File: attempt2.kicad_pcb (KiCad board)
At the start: 2 copper layers, 72 x 58.8 mm, 71 parts, among them J1 SIM_Card, J3 U.FL-R-SMT-110, J4 USB_C_Receptacle_USB2.0_14P, J5 U.FL-R-SMT-110, SW3 SW_Push, SW4 SW_Push, U1 nRF9160-SIxA, U2 TPD3F303DPVR, U3 MCP73831T-2ACI_OT, U4 MIC94092YC6-TR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

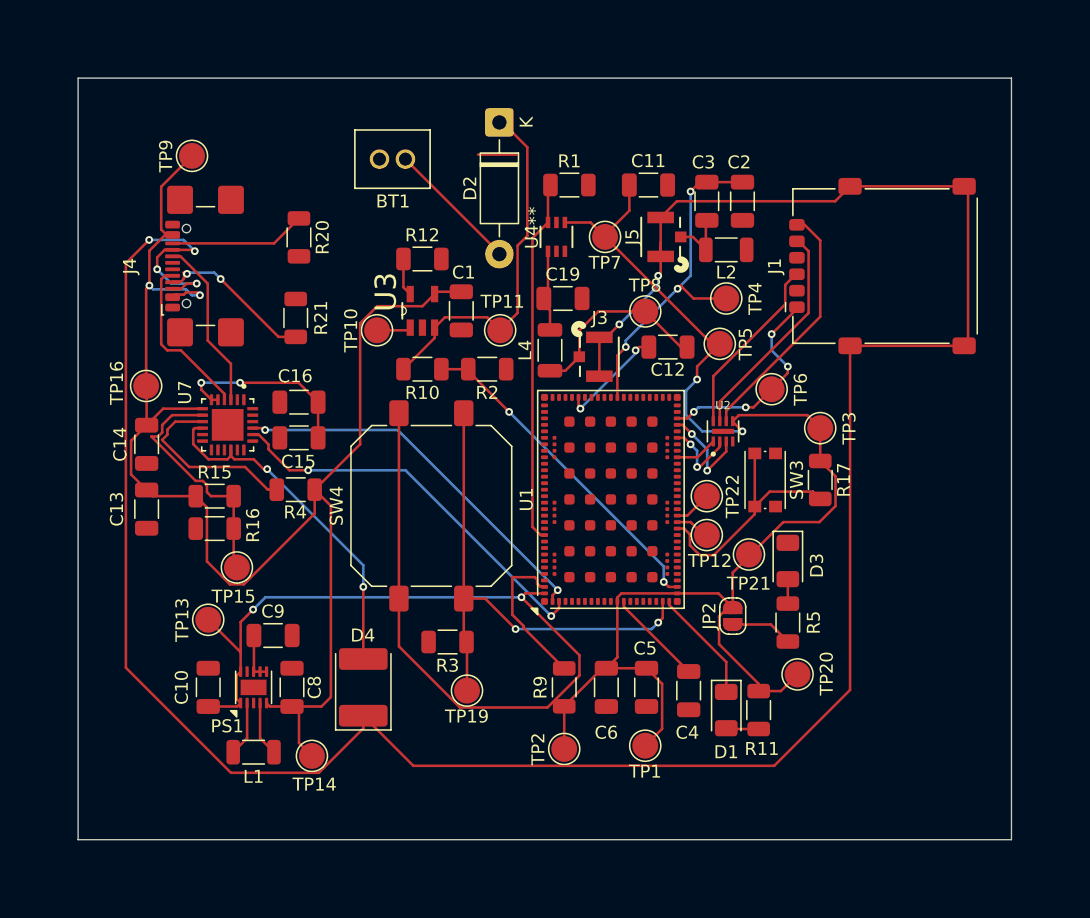
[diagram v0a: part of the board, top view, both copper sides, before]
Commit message: flipped direction of usb and moved antennas to edge
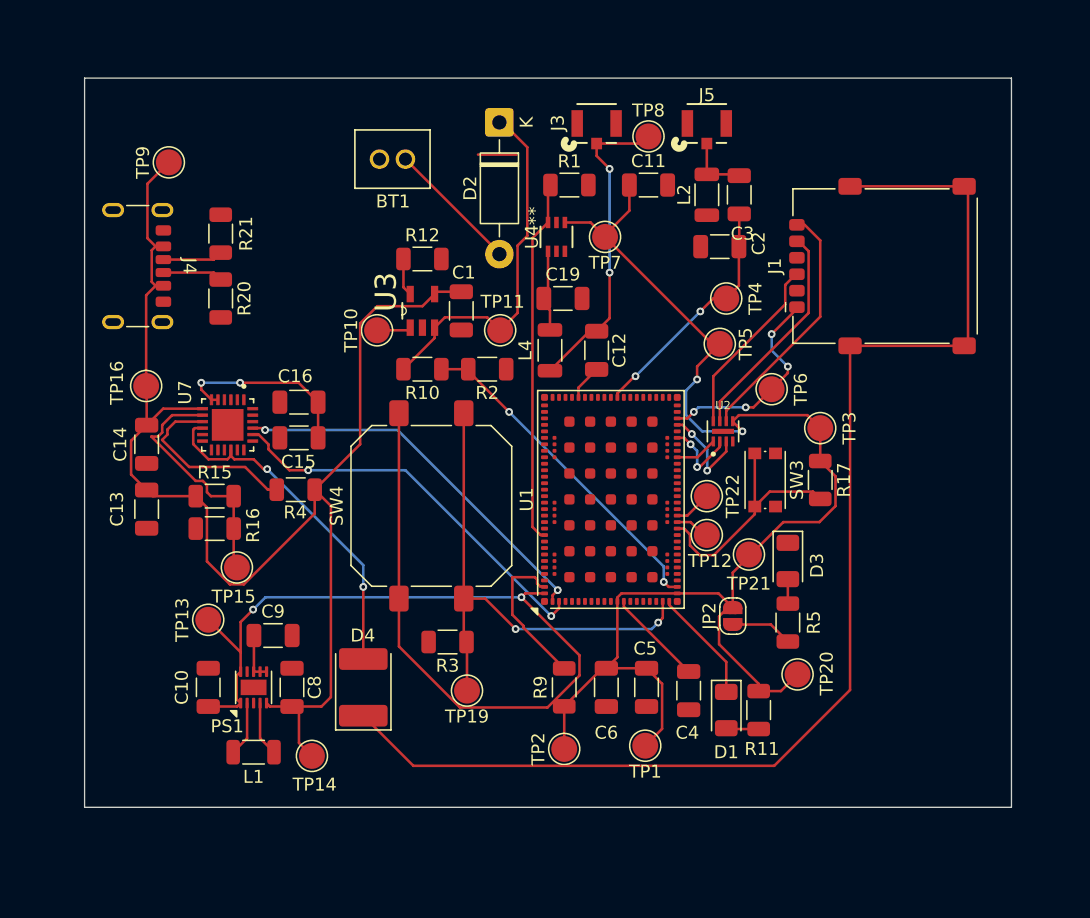
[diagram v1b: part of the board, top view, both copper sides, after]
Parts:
- J4: footprint Connector_USB:USB_C_Receptacle_GCT_USB4110 -> Connector_USB:USB_C_Receptacle_GCT_USB4125-xx-x-0190_6P_TopMnt_Horizontal
- R10, R2: value R -> 100k
- R11, R5: value R -> 500k
- R15: value 100k -> 22k
- R16: value 100k -> 33k
- R17: value 100k -> 1k
- R3: value 100k -> 10k
- R9: value 1M -> 10k
- moved J3 18.0 mm to (140.5, 82.0), turned to 0 degrees
- moved TP8 13.5 mm to (144.5, 83.0)
- moved J5 9.45 mm to (149.0, 82.0), turned to 0 degrees
- moved R21 8.70 mm to (111.5, 90.5)
- moved R20 7.66 mm to (111.5, 95.5)
- moved J4 7.47 mm to (104.0, 93.0), turned to -90 degrees
- moved C12 5.51 mm to (140.5, 99.5), turned to 90 degrees
- moved L2 4.51 mm to (149.0, 87.5), turned to -90 degrees
- moved C2 3.91 mm to (150.0, 91.5), turned to 180 degrees
- moved C3 2.55 mm to (151.5, 87.5), turned to -90 degrees
- moved TP9 1.86 mm to (107.5, 85.0)
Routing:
- net (no net): track 227.5 -> 125.1 mm, vias 8 -> 2
- net DIFF_P: track 13.3 -> 0.00 mm
- net DIFF_N: track 12.9 -> 0.00 mm
- net Net-(C12-Pad2): track 14.8 -> 24.4 mm, vias 0 -> 2
- net Net-(U1-ANT): track 26.8 -> 18.7 mm, vias 3 -> 2
- net Net-(J4-CC1): track 12.5 -> 4.64 mm, vias 2 -> 0
- net VBUS: track 112.7 -> 105.6 mm, vias 2 -> 0
- net Net-(J4-CC2): track 10.5 -> 4.64 mm
- net GPS: track 8.43 -> 2.73 mm, vias 2 -> 0
- net Net-(C3-Pad1): track 4.26 -> 4.92 mm
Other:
- board size 72 x 58.8 mm -> 71.5 x 56.2 mm

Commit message: worked on erc and drc errors
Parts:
- removed C11: C, Capacitor_SMD:C_1206_3216Metric
- removed TP5, TP6: TestPoint, TestPoint:TestPoint_Pad_D2.0mm
- added C7: 100n, Capacitor_SMD:C_1206_3216Metric, F.Cu at (164.0, 101.5)
- J1: footprint Connector_Card:nanoSIM_GCT_SIM8060-6-1-14-00 -> Connector_Card:nanoSIM_GCT_SIM8060-6-0-14-00
- J4: footprint Connector_USB:USB_C_Receptacle_GCT_USB4125-xx-x-0190_6P_TopMnt_Horizontal -> Connector_USB:USB_C_Receptacle_GCT_USB4110
- R10, R2: value 100k -> R
- R11, R5: value 500k -> R
- R15: value 22k -> 100k
- R16: value 33k -> 100k
- R17: value 1k -> 100k
- R3: value 10k -> 100k
- R9: value 10k -> 1M
- moved R20 1.50 mm to (113.0, 95.5)
- moved R21 1.50 mm to (113.0, 90.5)
- moved TP9 1.50 mm to (107.5, 83.5)
- turned U2 to 180 degrees
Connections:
- U2 pad 1: Net-(U1-SIM_RST) -> Net-(J1-RST)
- U2 pad 2: Net-(U1-SIM_CLK) -> Net-(J1-CLK)
- U2 pad 3: Net-(U1-SIM_IO) -> Net-(J1-I/O)
- U2 pad 5: VSYS -> Net-(J1-VCC)
- U2 pad 6: Net-(J1-I/O) -> Net-(U1-SIM_IO)
- U2 pad 7: Net-(J1-CLK) -> Net-(U1-SIM_CLK)
- U2 pad 8: Net-(J1-RST) -> Net-(U1-SIM_RST)
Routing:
- net GND: track 3.00 -> 161.7 mm, vias 0 -> 23
- net DIFF_N: track 0.00 -> 15.8 mm, vias 0 -> 2
- net DIFF_P: track 0.00 -> 14.9 mm, vias 0 -> 2
- net VSYS: track 184.6 -> 172.0 mm
- net Net-(J1-VCC): track 16.4 -> 24.9 mm, vias 4 -> 6
- net VBUS: track 105.6 -> 110.5 mm
- net Net-(U1-SIM_IO): track 7.59 -> 2.85 mm, vias 2 -> 0
- net Net-(U1-SIM_CLK): track 6.01 -> 2.85 mm, vias 2 -> 0
- net Net-(J1-RST): track 14.1 -> 17.1 mm
- net Net-(J1-CLK): track 17.2 -> 18.5 mm, vias 0 -> 2
- net Net-(PS1-EN): track 3.80 -> 4.94 mm
- net Net-(J4-CC2): track 4.64 -> 5.62 mm
- net Net-(U7-VDD): track 14.5 -> 15.4 mm
- net Net-(J4-CC1): track 4.64 -> 5.41 mm
- net Net-(J1-I/O): track 19.3 -> 19.9 mm

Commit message: final cleanup before design review
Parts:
- C7: value 100n -> 1n
- R20: value 1.5k -> 5.1k
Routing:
- net DIFF_P: track 14.9 -> 17.3 mm
- net GND: track 161.7 -> 159.5 mm
- net DIFF_N: track 15.8 -> 17.2 mm, vias 2 -> 4
- net VBUS: track 110.5 -> 109.2 mm

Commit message: FINAL BEFORE ANDREW
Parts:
- removed TP12: SWDCLK, TestPoint:TestPoint_Pad_D2.0mm
- removed TP22: SWDIO, TestPoint:TestPoint_Pad_D2.0mm
- added J2: Conn_01x05_Pin, Connector_PinSocket_2.54mm:PinSocket_1x05_P2.54mm_Vertical, F.Cu at (163.0, 115.7)
- R15: value 100k -> 22k
- R16: value 100k -> 33k
- moved R17 1.25 mm to (156.5, 109.5)
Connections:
- R17 pad 2: Net-(U1-~{RESET}) -> Net-(J2-Pin_5)
- SW3 pad 1: GND -> Net-(J2-Pin_5)
- SW3 pad 2: Net-(U1-~{RESET}) -> GND
- U1 pad 32: Net-(U1-~{RESET}) -> Net-(J2-Pin_5)
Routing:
- net Net-(J2-Pin_5): track 0.00 -> 26.0 mm, vias 0 -> 2
- net Net-(U1-~{RESET}): track 19.1 -> 0.00 mm
- net Net-(J2-Pin_4): track 2.90 -> 18.0 mm, vias 0 -> 2
- net Net-(J2-Pin_2): track 2.80 -> 16.5 mm, vias 0 -> 2
- net VSYS: track 172.0 -> 181.5 mm, vias 4 -> 6
- net GND: track 159.5 -> 165.1 mm, vias 23 -> 24
- net DIFF_N: track 17.2 -> 19.5 mm
- net VBUS: track 109.2 -> 110.3 mm
- net DIFF_P: track 17.3 -> 18.0 mm
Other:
- board text added: "STAT BOARD v1.0"

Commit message: fixed resistor values
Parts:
- R10, R2: value R -> 100k
- R11, R5: value R -> 500
- R17: value 100k -> 1k
- R3: value 100k -> 4.7k
- R9: value 1M -> 10k
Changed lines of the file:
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@@
 			)
 		)
-		(property "Value" "R"
+		(property "Value" "100k"
 			(at 0 1.83 0)
 			(layer "F.Fab")
@@
 			)
 		)
-		(property "Value" "100k"
+		(property "Value" "4.7k"
 			(at 0 1.83 0)
 			(layer "F.Fab")
@@
 			)
 		)
-		(property "Value" "R"
+		(property "Value" "100k"
 			(at 0 1.83 0)
 			(layer "F.Fab")
@@
 			)
 		)
-		(property "Value" "R"
+		(property "Value" "500"
 			(at 0 1.83 90)
 			(layer "F.Fab")
@@
 			)
 		)
-		(property "Value" "100k"
+		(property "Value" "1k"
 			(at 0 1.83 90)
 			(layer "F.Fab")
@@
 			)
 		)
-		(property "Value" "R"
+		(property "Value" "500"
 			(at 0 1.83 90)
 			(layer "F.Fab")
@@
 			)
 		)
-		(property "Value" "1M"
+		(property "Value" "10k"
 			(at 0 1.83 90)
 			(layer "F.Fab")

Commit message: rah
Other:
- board text added: "STAT BOARD 8/2/2025 v1.0"
- board text removed: "STAT BOARD v1.0"
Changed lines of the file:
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@@
 	)
 	(paper "A4")
+	(title_block
+		(title "STAT BOARD")
+		(date "2025-08-02")
+		(rev "v1.0")
+		(company "XIBIDI TECHNOLOGIES")
+	)
 	(layers
 		(0 "F.Cu" signal)
@@
 		(layer "Edge.Cuts")
 	)
-	(gr_text "STAT BOARD\nv1.0"
+	(gr_text "STAT BOARD\n8/2/2025\nv1.0"
 		(at 170.5 133 0)
 		(layer "F.SilkS")

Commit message: Schematic design review, remove 3.3V switcher and run right off battery, re-arrange schematic for easier reading, moved to four layer PCB because RF, cleaned up zones, including adding vbat zone. Plenty left to do, see design review notes.
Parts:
- removed C10: 100u, Capacitor_SMD:C_1206_3216Metric
- removed C8: 10u, Capacitor_SMD:C_1206_3216Metric
- removed C9: 100p, Capacitor_SMD:C_1206_3216Metric
- removed D2: SB120, Diode_THT:D_DO-41_SOD81_P10.16mm_Horizontal
- removed D4: BAT20JFILM, Diode_SMD:D_2114_3652Metric
- removed L1: 1.5u, Inductor_SMD:L_1206_3216Metric
- removed PS1: TPS63031DSKR, Package_SON:WSON-10-1EP_2.5x2.5mm_P0.5mm_EP1.2x2mm
- removed R15: 22k, Resistor_SMD:R_1206_3216Metric
- removed R16: 33k, Resistor_SMD:R_1206_3216Metric
- removed R17: 1k, Resistor_SMD:R_1206_3216Metric
- removed TP13, TP14, TP8: TestPoint, TestPoint:TestPoint_Pad_D2.0mm
- added C11: 100n, Capacitor_SMD:C_1206_3216Metric, F.Cu at (95.8, 110.8)
- BT1: value Battery_Cell -> 1528-2731-ND
- R11, R5: value 500 -> 2k
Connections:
- BT1 pad 1: Net-(BT1-+) -> +3V8
- C5 pad 1: VSYS -> +3V8
- C6 pad 1: VSYS -> +3V8
- J2 pad 1: VSYS -> +3V8
- J4 pad S1: GND -> Net-(J4-SHIELD)
- JP2 pad 2: VSYS -> +3V8
- R10 pad 2: VBAT -> +3V8
- R11 pad 1: VSYS -> +3V8
- R9 pad 1: VSYS -> +3V8
- SW4 pad 1: VSYS -> +3V8
- TP1 pad 1: VSYS -> +3V8
- TP11 pad 1: VBAT -> +3V8
- TP15 pad 1: Net-(U7-VBUS) -> VBUS
- TP2 pad 1: VSYS -> +3V8
- TP20 pad 1: VSYS -> +3V8
- TP21 pad 1: VSYS -> +3V8
- TP3 pad 1: VSYS -> Net-(J2-Pin_5)
- TP7 pad 1: VSYS -> +3V8
- U1 pad 102: VSYS -> +3V8
- U1 pad 12: VSYS -> +3V8
- U1 pad 22: VSYS -> +3V8
- U3 pad 3: VBAT -> +3V8
- U4 pad 4: VSYS -> +3V8
- U7 pad 8: Net-(U7-VBUS) -> VBUS
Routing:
- net VSYS: track 181.5 -> 0.00 mm, vias 6 -> 0
- net (no net): track 125.1 -> 209.0 mm
- net VBAT: track 27.9 -> 0.00 mm
- net +3V8: track 0.00 -> 19.2 mm, vias 0 -> 6
- net Net-(U7-VBUS): track 19.2 -> 0.00 mm
- net Net-(BT1-+): track 10.6 -> 0.00 mm
- net GND: track 165.1 -> 155.2 mm, vias 24 -> 32
- net VBUS: track 110.3 -> 105.1 mm
- net Net-(PS1-EN): track 4.94 -> 0.00 mm
- net Net-(PS1-L1): track 4.48 -> 0.00 mm
- net Net-(PS1-L2): track 4.23 -> 0.00 mm
- net DIFF_N: track 19.5 -> 15.6 mm, vias 4 -> 2
- added copper zone on In2.Cu, net +3V8
- added copper zone on In1.Cu, net GND
- added copper zone on In2.Cu, net GND
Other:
- copper layers 2 -> 4

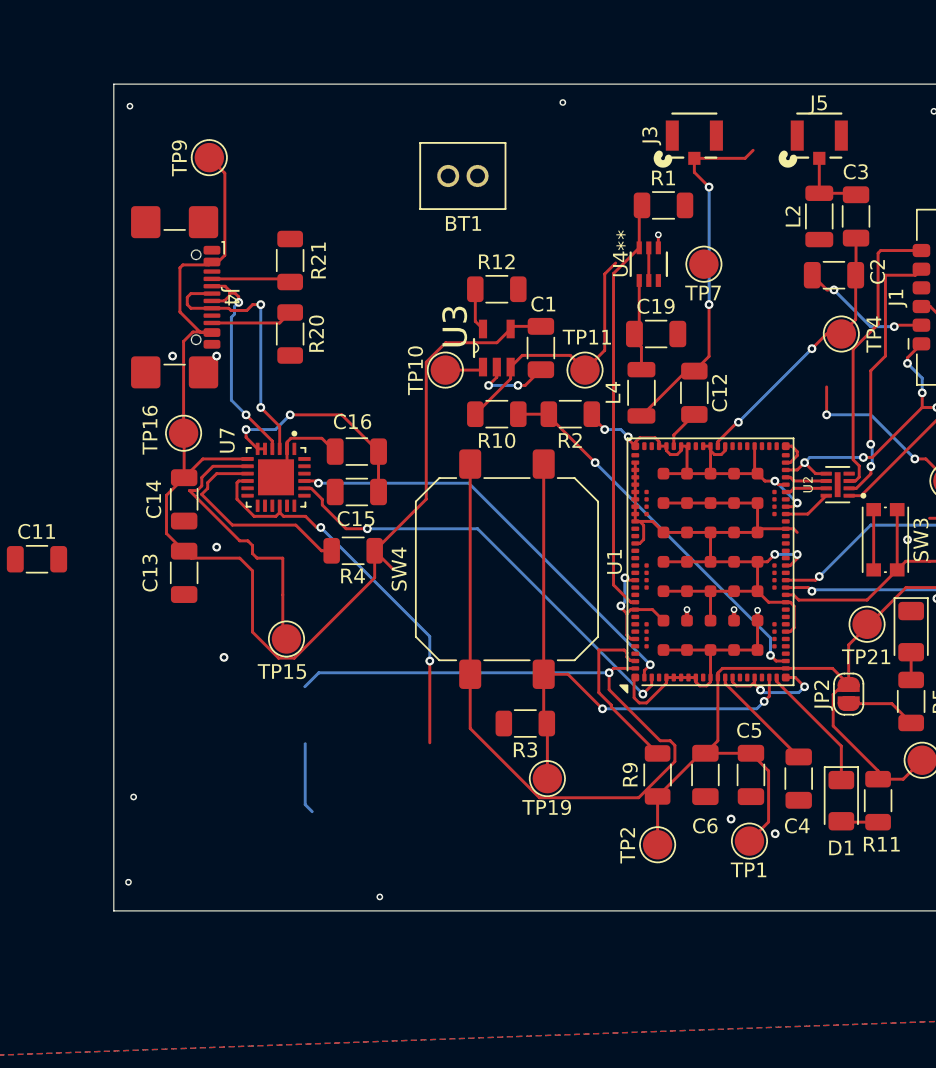
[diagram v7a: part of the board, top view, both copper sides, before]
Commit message: changed gps antenna lte antenna xibidi and other thins too
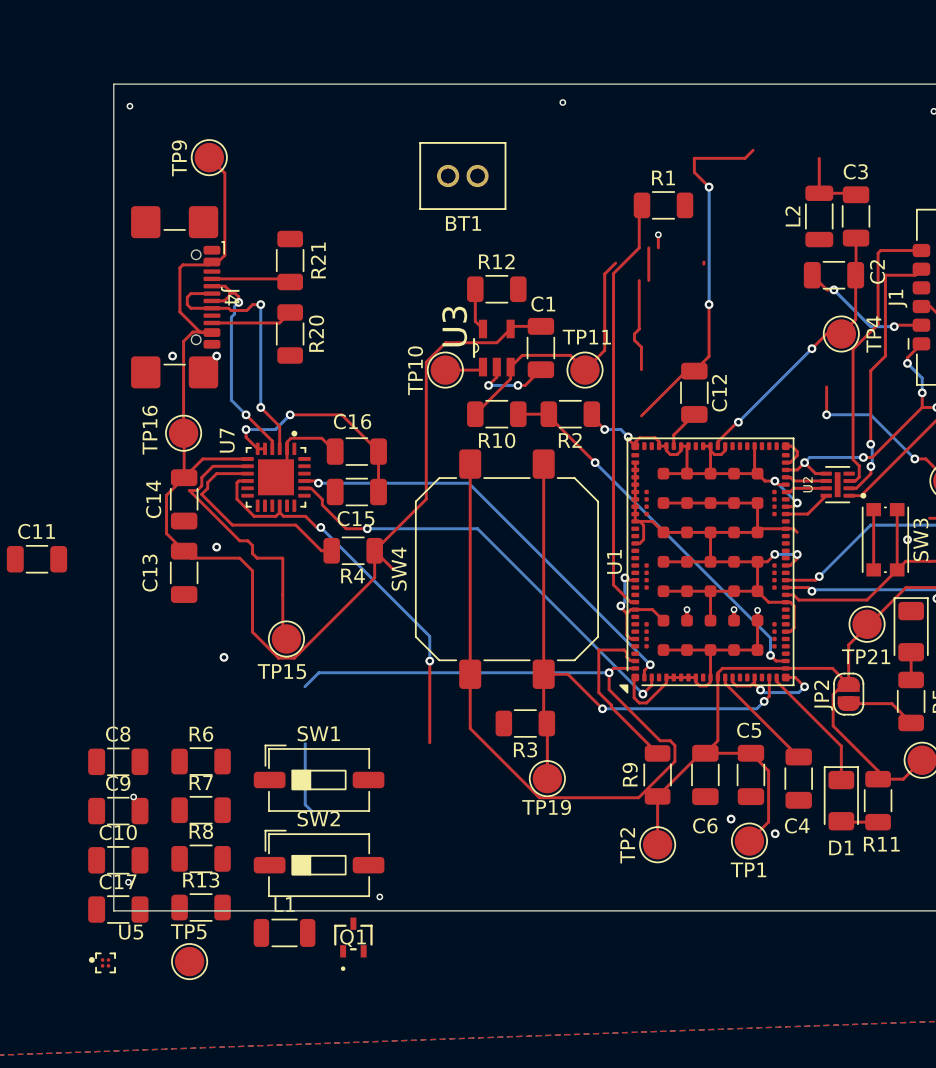
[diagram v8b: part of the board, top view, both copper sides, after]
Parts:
- removed C19: 56p, Capacitor_SMD:C_1206_3216Metric
- removed J3, J5: U.FL-R-SMT-110, footprints:CONN1_UFL-R_HIR
- removed L4: 68n, Inductor_SMD:L_1206_3216Metric
- removed TP7: TestPoint, TestPoint:TestPoint_Pad_D2.0mm
- removed U4: MIC94092YC6-TR, footprints:SC-70-6_C6_MCH
- added C10: 47u, Capacitor_SMD:C_1206_3216Metric, F.Cu at (101.3, 131.3)
- added C17: 4.7u, Capacitor_SMD:C_1206_3216Metric, F.Cu at (101.3, 134.7)
- added C8: 100nF, Capacitor_SMD:C_1206_3216Metric, F.Cu at (101.3, 124.6)
- added C9: 10p, Capacitor_SMD:C_1206_3216Metric, F.Cu at (101.3, 128.0)
- added L1: 7.3n, Inductor_SMD:L_1206_3216Metric, F.Cu at (112.6, 136.2)
- added Q1: PMOS, footprints_mosfet:SOT-323-3_2P2X1P35_ONS-L, F.Cu at (117.3, 136.6)
- added R13: 10k, Resistor_SMD:R_1206_3216Metric, F.Cu at (106.9, 134.5)
- added R6: 25k, Resistor_SMD:R_1206_3216Metric, F.Cu at (106.9, 124.6)
- added R7: 50, Resistor_SMD:R_1206_3216Metric, F.Cu at (106.9, 127.9)
- added R8: 50, Resistor_SMD:R_1206_3216Metric, F.Cu at (106.9, 131.2)
- added SW1: SW_DPST_x2, Button_Switch_SMD:SW_DIP_SPSTx01_Slide_6.7x4.1mm_W6.73mm_P2.54mm_LowProfile_JPin, F.Cu at (115.0, 125.8)
- added SW2: SW_DPST_x2, Button_Switch_SMD:SW_DIP_SPSTx01_Slide_6.7x4.1mm_W6.73mm_P2.54mm_LowProfile_JPin, F.Cu at (115.0, 131.6)
- added TP5: TestPoint, TestPoint:TestPoint_Pad_D2.0mm, F.Cu at (106.2, 138.2)
- added U5: MAX2686LEWS_, MAX2686LEWS_:BGA4N40P2X2_84X84X69N, F.Cu at (100.4, 138.3)
- C12: value 56p -> 100n
- C5: value 4.7u -> 15p
- C6: value 4.7u -> 100n
- J2: value Conn_01x05_Pin -> Conn_02x05_Pin
- R1: value 100K -> 10k
- R12: value 2k -> 2.5k
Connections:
- net DIFF_N renamed DN
- net DIFF_P renamed DP
- C12 pad 1: GPS -> +3V8
- C12 pad 2: Net-(C12-Pad2) -> GND
- J2 pad 3: GND -> unconnected-(J2-Pin_3-Pad3)
- J2 pad 5: Net-(J2-Pin_5) -> +3V8
- R1 pad 1: COEX0 -> Net-(J2-Pin_10)
- R1 pad 2: GND -> Net-(U1-~{RESET})
- R10 pad 2: +3V8 -> Net-(SW2A-B)
- SW3 pad 1: Net-(J2-Pin_5) -> Net-(U1-~{RESET})
- TP3 pad 1: Net-(J2-Pin_5) -> Net-(U1-~{RESET})
- U1 pad 32: Net-(J2-Pin_5) -> Net-(U1-~{RESET})
- U1 pad 33: Net-(J2-Pin_2) -> Net-(J2-Pin_4)
- U1 pad 34: Net-(J2-Pin_4) -> Net-(J2-Pin_2)
- U1 pad 55: unconnected-(U1-MAGPIO0-Pad55) -> GPIO
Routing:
- net +3V8: track 19.2 -> 197.3 mm, vias 6 -> 8
- net (no net): track 209.0 -> 63.3 mm
- net Net-(J2-Pin_5): track 26.0 -> 0.00 mm, vias 2 -> 0
- net GND: track 155.2 -> 179.6 mm, vias 32 -> 34
- net Net-(C12-Pad2): track 24.4 -> 0.00 mm, vias 2 -> 0
- net Net-(U4-VOUT): track 6.40 -> 0.00 mm
